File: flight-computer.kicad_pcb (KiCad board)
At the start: 2 copper layers, 50 parts, among them J1 Throttle/BEC, J2 Servo 1, J3 Servo 2, J4 Servo 3, J5 Servo 4, J6 Breakout1, J7 Power, J8 Ext, J9 Breakout2, SW1 SW_Push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

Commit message: Board outline
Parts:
- moved R17 105.7 mm to (96.4, 106.7)
- moved R13 94.4 mm to (121.7, 60.4), turned to 270 degrees
- moved C8 84.4 mm to (104.0, 103.2), turned to 270 degrees
- moved R14 82.9 mm to (122.9, 60.4), turned to 90 degrees
- moved C6 81.8 mm to (105.3, 103.2), turned to 270 degrees
- moved J9 80.9 mm to (130.5, 78.0)
- moved C4 79.3 mm to (106.6, 103.2), turned to 270 degrees
- moved J6 79.1 mm to (126.0, 78.0)
- moved R12 78.8 mm to (124.2, 60.4), turned to 270 degrees
- moved C7 76.8 mm to (107.8, 103.2), turned to 270 degrees
- moved R8 76.7 mm to (131.8, 60.4), turned to 180 degrees
- moved C3 76.3 mm to (131.8, 65.5), turned to 270 degrees
- moved R7 74.8 mm to (122.9, 63.0), turned to 270 degrees
- moved R9 73.7 mm to (131.8, 63.0), turned to 180 degrees
- moved C2 72.7 mm to (133.1, 65.5), turned to 270 degrees
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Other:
- board outline added: 50 x 62 mm

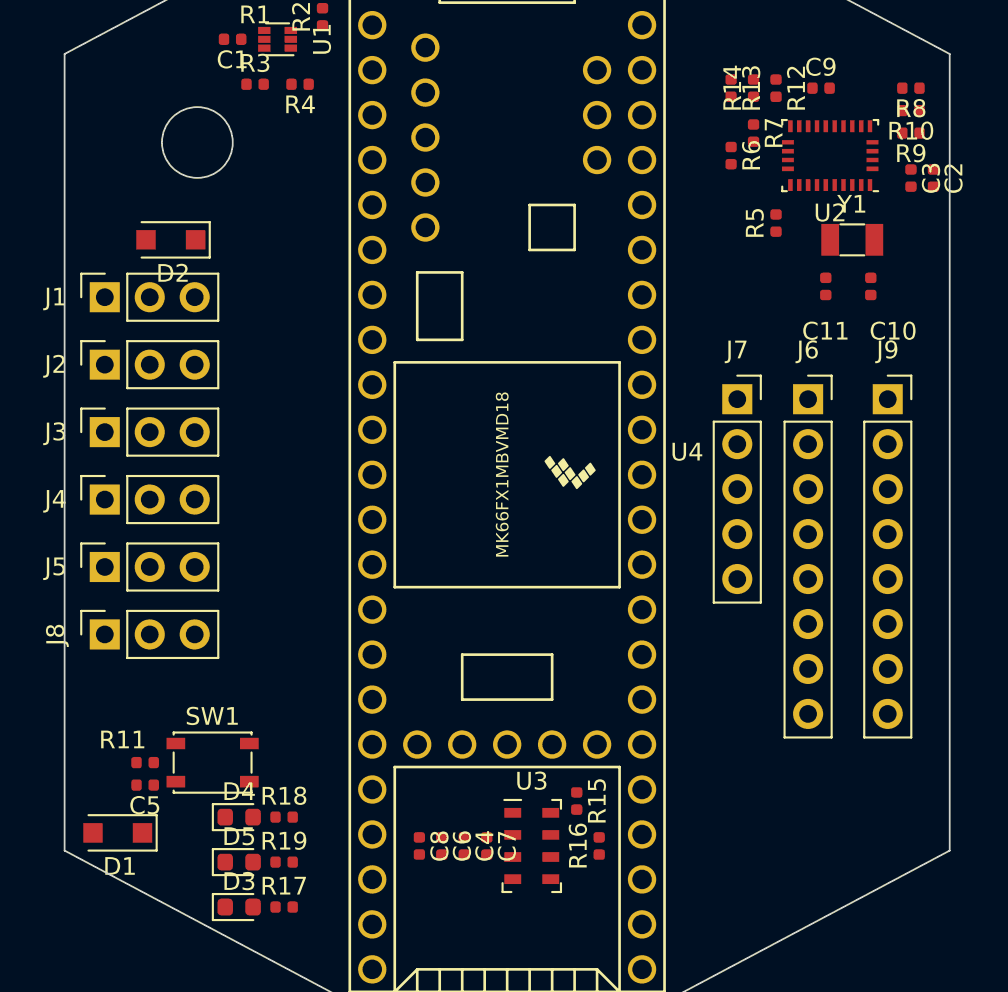
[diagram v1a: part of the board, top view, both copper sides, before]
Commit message: Added holes
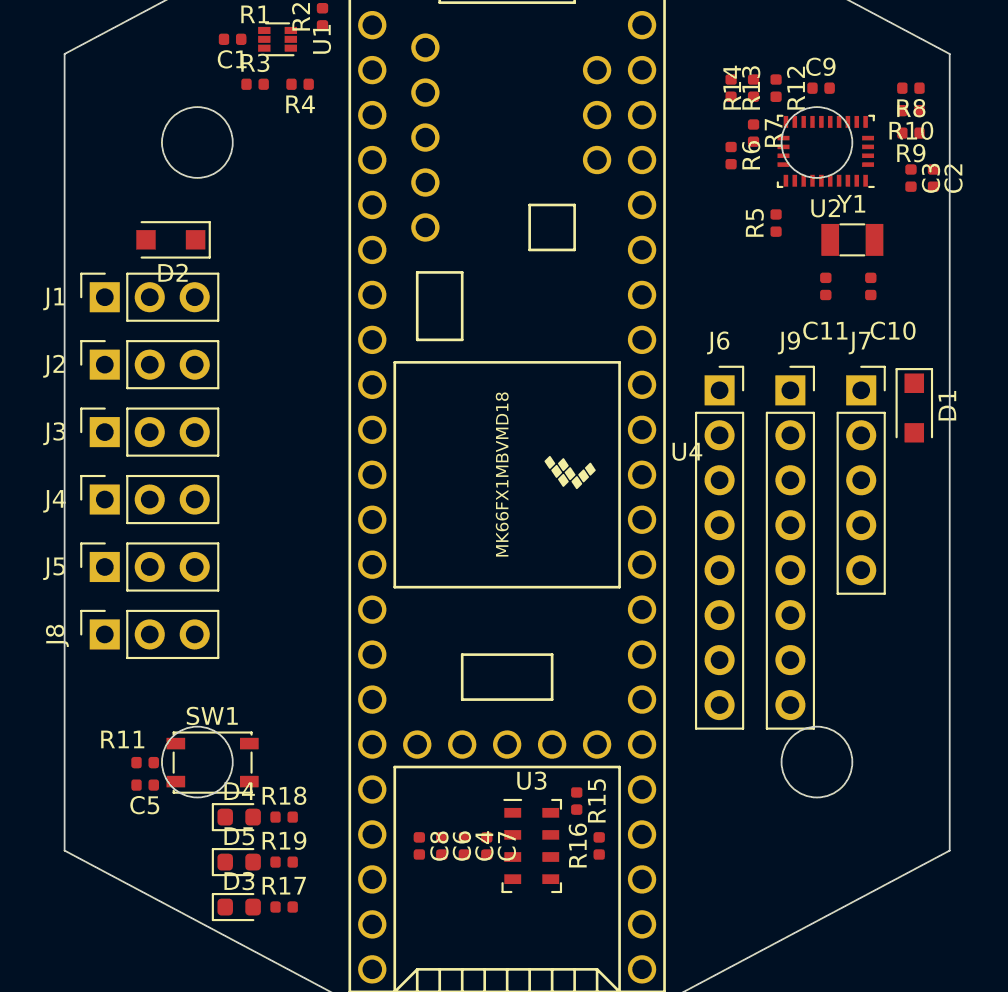
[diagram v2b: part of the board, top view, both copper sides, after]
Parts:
- moved D1 51.0 mm to (132.0, 78.5), turned to 270 degrees
- moved J7 7.02 mm to (129.0, 77.5)
- moved J9 5.52 mm to (125.0, 77.5)
- moved J6 5.02 mm to (121.0, 77.5)
- moved U2 0.35 mm to (127.0, 64.0)
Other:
- outline, holes or cut-outs redrawn
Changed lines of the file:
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@@
   (general
     (thickness 1.6)
-    (drawings 9)
+    (drawings 12)
     (tracks 0)
     (zones 0)
@@
   )
   (module Diode_SMD:D_SOD-123F (layer F.Cu)
-    (at 87 102.5 180)
+    (at 132 78.5 270)
     (descr D_SOD-123F)
     (tags D_SOD-123F)
     (attr smd)
-    (fp_text reference D1 (at -0.127 -1.905) (layer F.SilkS)
-      (effects (font (size 1 1) (thickness 0.15)))
-    )
-    (fp_text value SS14FL (at 0 2.1) (layer F.Fab)
-      (effects (font (size 1 1) (thickness 0.15)))
-    )
-    (fp_text user %R (at -0.127 -1.905) (layer F.Fab)
+    (fp_text reference D1 (at -0.127 -1.905 90) (layer F.SilkS)
+      (effects (font (size 1 1) (thickness 0.15)))
+    )
+    (fp_text value SS14FL (at 0 2.1 90) (layer F.Fab)
+      (effects (font (size 1 1) (thickness 0.15)))
+    )
+    (fp_text user %R (at -0.127 -1.905 90) (layer F.Fab)
       (effects (font (size 1 1) (thickness 0.15)))
     )
@@
     (fp_line (start -2.2 1) (end 1.65 1) (layer F.SilkS) (width 0.12))
     (fp_line (start -2.2 -1) (end 1.65 -1) (layer F.SilkS) (width 0.12))
-    (pad 1 smd rect (at -1.4 0 180) (size 1.1 1.1) (layers F.Cu F.Paste F.Mask)
+    (pad 1 smd rect (at -1.4 0 270) (size 1.1 1.1) (layers F.Cu F.Paste F.Mask)
       (net 8 /VIN))
-    (pad 2 smd rect (at 1.4 0 180) (size 1.1 1.1) (layers F.Cu F.Paste F.Mask)
+    (pad 2 smd rect (at 1.4 0 270) (size 1.1 1.1) (layers F.Cu F.Paste F.Mask)
       (net 9 /VEXT))
     (model ${KISYS3DMOD}/Diode_SMD.3dshapes/D_SOD-123F.wrl
@@
   )
   (module Connector_PinSocket_2.54mm:PinSocket_1x08_P2.54mm_Vertical (layer F.Cu)
-    (at 126 78)
+    (at 121 77.5)
     (descr "Through hole straight socket strip, 1x08, 2.54mm pitch, single row (from Kicad 4.0.7), script generated")
     (tags "Through hole socket strip THT 1x08 2.54mm single row")
@@
   )
   (module Connector_PinSocket_2.54mm:PinSocket_1x05_P2.54mm_Vertical (layer F.Cu)
-    (at 122 78)
+    (at 129 77.5)
     (descr "Through hole straight socket strip, 1x05, 2.54mm pitch, single row (from Kicad 4.0.7), script generated")
     (tags "Through hole socket strip THT 1x05 2.54mm single row")
@@
   )
   (module Connector_PinSocket_2.54mm:PinSocket_1x08_P2.54mm_Vertical (layer F.Cu)
-    (at 130.5 78)
+    (at 125 77.5)
     (descr "Through hole straight socket strip, 1x08, 2.54mm pitch, single row (from Kicad 4.0.7), script generated")
     (tags "Through hole socket strip THT 1x08 2.54mm single row")
@@
   )
   (module Package_LGA:LGA-28_5.2x3.8mm_P0.5mm (layer F.Cu)
-    (at 127.25 64.24 180)
+    (at 127 64 180)
     (descr "LGA 28 5.2x3.8mm Pitch 0.5mm")
     (tags "LGA 28 5.2x3.8mm Pitch 0.5mm")
@@
     )
   )
+  (gr_circle (center 126.5 98.5) (end 128.5 98.5) (layer Edge.Cuts) (width 0.1))
+  (gr_circle (center 126.5 63.5) (end 128.5 63.5) (layer Edge.Cuts) (width 0.1))
+  (gr_circle (center 91.5 98.5) (end 93.5 98.5) (layer Edge.Cuts) (width 0.1))
   (gr_circle (center 91.5 63.5) (end 93.5 63.5) (layer Edge.Cuts) (width 0.1))
   (gr_line (start 134 58.5) (end 134 103.5) (layer Edge.Cuts) (width 0.1))

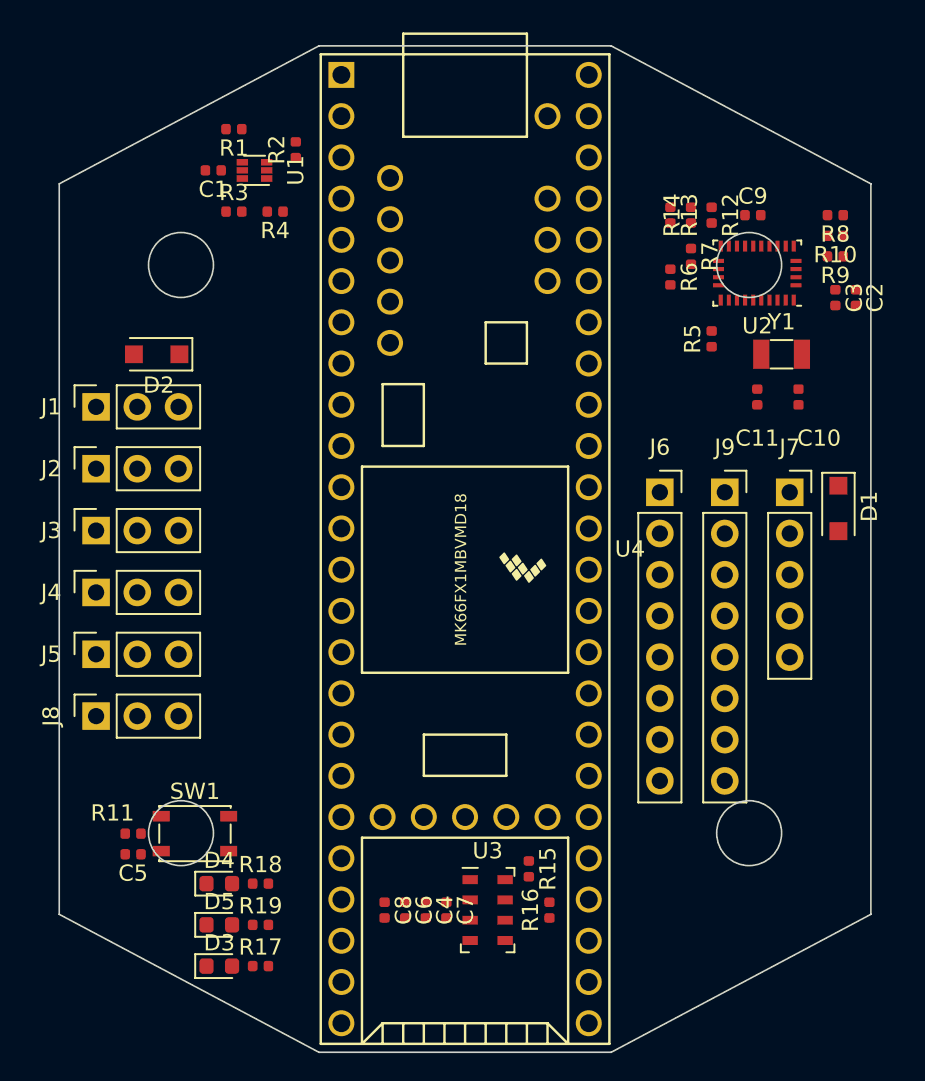
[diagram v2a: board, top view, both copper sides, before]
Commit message: New crystal footprint, layout changes
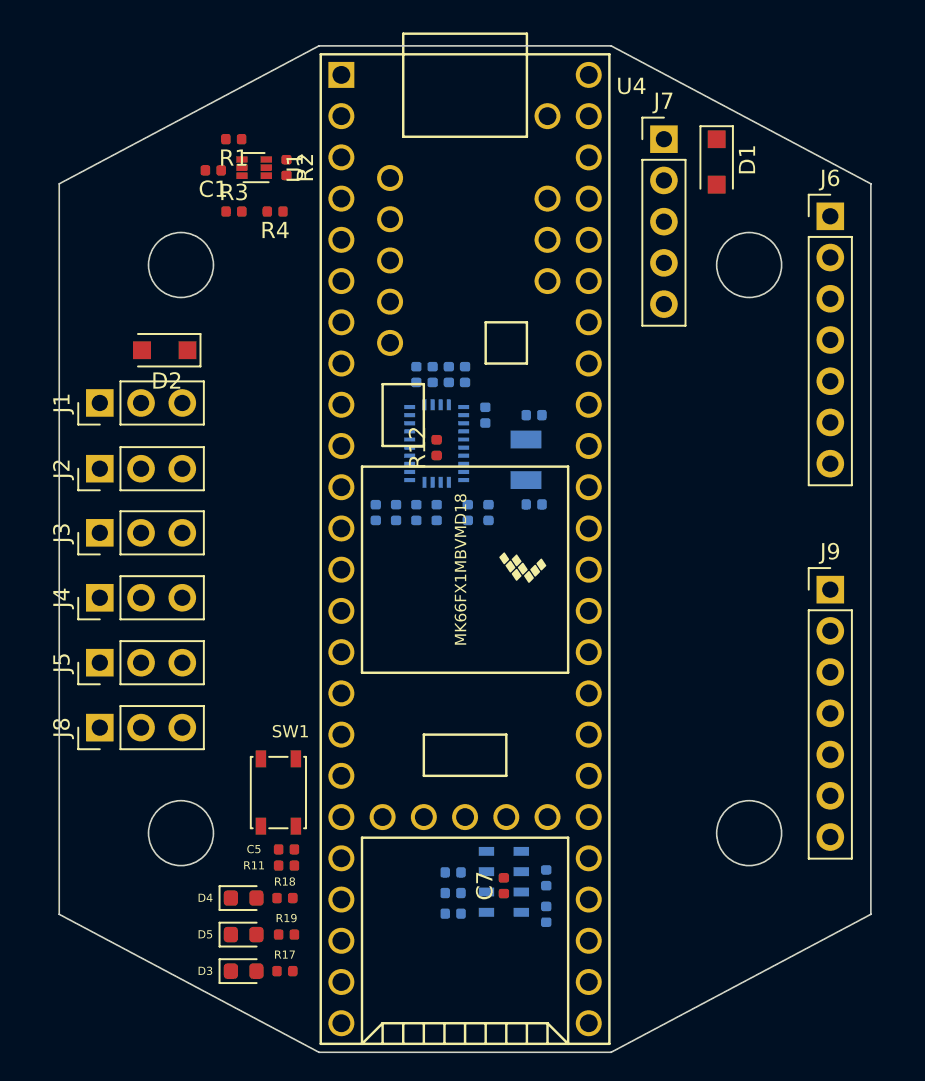
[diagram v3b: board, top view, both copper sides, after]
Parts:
- C10, C11, C2, C3, C4, C6, C8, C9, R10, R13, R14, R15, R16, R5, R6, R7, R8, R9, U2, U3: moved to B.Cu
- J1, J2, J3, J4, J5, J8: footprint Connector_PinSocket_2.54mm:PinSocket_1x03_P2.54mm_Vertical -> Connector_PinHeader_2.54mm:PinHeader_1x03_P2.54mm_Vertical
- J6, J9: footprint Connector_PinSocket_2.54mm:PinSocket_1x08_P2.54mm_Vertical -> Connector_PinHeader_2.54mm:PinHeader_1x07_P2.54mm_Vertical
- J7: footprint Connector_PinSocket_2.54mm:PinSocket_1x05_P2.54mm_Vertical -> Connector_PinHeader_2.54mm:PinHeader_1x05_P2.54mm_Vertical
- Y1: footprint Crystal:Crystal_SMD_3215-2Pin_3.2x1.5mm -> flight-computer:ABS07; moved to B.Cu
- moved R8 32.7 mm to (104.8, 78.8), turned to 90 degrees
- moved R10 30.9 mm to (106.0, 78.8), turned to 90 degrees
- moved C9 29.6 mm to (103.5, 78.8), turned to 90 degrees
- moved R9 29.2 mm to (107.2, 78.8), turned to 90 degrees
- moved C2 27.3 mm to (109.2, 78.8)
- moved C3 25.1 mm to (110.4, 78.8)
- moved J7 23.1 mm to (121.2, 55.8)
- moved D1 22.6 mm to (124.5, 57.1)
- moved U2 22.4 mm to (107.2, 74.5), turned to 90 degrees
- moved R12 22.2 mm to (107.2, 74.8), turned to 90 degrees
- moved J6 20.0 mm to (131.5, 60.5)
- moved R14 19.6 mm to (106.0, 70.2)
- moved R13 17.6 mm to (107.0, 70.2)
- moved C10 17.6 mm to (113.2, 78.2), turned to 180 degrees
- moved Y1 17.0 mm to (112.8, 75.5), turned to 270 degrees
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
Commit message: Routing
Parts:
- removed D5: BLUE, LED_SMD:LED_0603_1608Metric
- C1, R1, R2, R3, R4, U1: moved to B.Cu
- D2: value SS14FL -> GREEN; footprint Diode_SMD:D_SOD-123F -> LED_SMD:LED_0603_1608Metric
- D3: value GREEN -> RED
- D4: value RED -> BLUE
- moved J6 42.0 mm to (91.5, 73.2)
- moved J1 40.0 mm to (126.5, 70.0)
- moved J3 40.0 mm to (126.5, 80.5)
- moved J4 40.0 mm to (126.5, 84.5)
- moved J5 40.0 mm to (126.5, 88.5)
- moved J8 40.0 mm to (126.5, 92.5)
- moved J2 40.0 mm to (126.5, 76.5)
- moved D2 34.1 mm to (95.5, 102.5), turned to 0 degrees
- moved R1 18.4 mm to (111.5, 63.2), turned to 270 degrees
- moved C1 17.5 mm to (109.6, 64.5), turned to 270 degrees
- moved D1 16.7 mm to (129.0, 73.2), turned to 0 degrees
- moved U1 14.5 mm to (109.8, 62.0), turned to 270 degrees
- moved J9 13.2 mm to (120.5, 90.8)
- moved R3 12.6 mm to (107.0, 63.2), turned to 90 degrees
- moved R2 12.0 mm to (109.8, 60.0), turned to 180 degrees
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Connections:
- D1 pad 2: /VEXT -> /VBEC
- D2 pad 1: /VIN -> GND
- D2 pad 2: /VBEC -> Net-(D2-Pad2)
- J7 pad 2: /VEXT -> /VBEC
- R17 pad 1: Net-(D3-Pad2) -> Net-(D2-Pad2)
- R18 pad 1: Net-(D4-Pad2) -> Net-(D3-Pad2)
- R19 pad 1: Net-(D5-Pad2) -> Net-(D4-Pad2)
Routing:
- net +3V3: track 0.00 -> 119.1 mm, vias 0 -> 5
- net /VIN: track 0.00 -> 49.2 mm
- net /D31: track 0.00 -> 43.6 mm
- net /D32: track 0.00 -> 41.4 mm, vias 0 -> 2
- net /D26: track 0.00 -> 34.0 mm, vias 0 -> 1
- net /VBEC: track 0.00 -> 25.3 mm
- net /D27: track 0.00 -> 22.1 mm, vias 0 -> 2
- net /ALT_INT_1: track 0.00 -> 16.5 mm, vias 0 -> 1
- net /ALT_INT_2: track 0.00 -> 16.0 mm, vias 0 -> 3
- net GNDA: track 0.00 -> 15.7 mm, vias 0 -> 1
- net /SCL0: track 0.00 -> 9.91 mm
- net /BTN: track 0.00 -> 9.74 mm
- net /SDA2: track 0.00 -> 8.60 mm
- net /SCL2: track 0.00 -> 8.39 mm
- net /DAC1: track 0.00 -> 7.94 mm, vias 0 -> 1
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
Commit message: Finished routing
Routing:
- net /EXT: track 0.00 -> 44.5 mm, vias 0 -> 1
- net /SER4: track 0.00 -> 41.6 mm, vias 0 -> 3
- net /TMP_INT: track 1.26 -> 41.9 mm, vias 0 -> 1
- net GND: track 0.00 -> 39.9 mm, vias 0 -> 22
- net /SER2: track 0.00 -> 35.8 mm, vias 0 -> 1
- net /SER3: track 0.00 -> 32.7 mm, vias 0 -> 1
- net /RX1: track 0.00 -> 30.6 mm
- net /TX1: track 0.00 -> 30.6 mm
- net /SCL2: track 8.39 -> 39.0 mm
- net /SER1: track 0.00 -> 28.4 mm, vias 0 -> 1
- net /THR: track 0.00 -> 26.4 mm
- net /SDA2: track 8.60 -> 34.2 mm, vias 0 -> 1
- net /IMU_INT: track 0.00 -> 17.5 mm
- net +3V3: track 119.1 -> 133.9 mm, vias 5 -> 8
- added copper zone on B.Cu, net GND
- added copper zone on F.Cu, net GND
